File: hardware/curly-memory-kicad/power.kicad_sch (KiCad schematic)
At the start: 19 parts, among them J501 Conn_02x05_Odd_Even, U501 NCP1117-5.0_SOT223, U502 NCP1117-3.3_SOT223

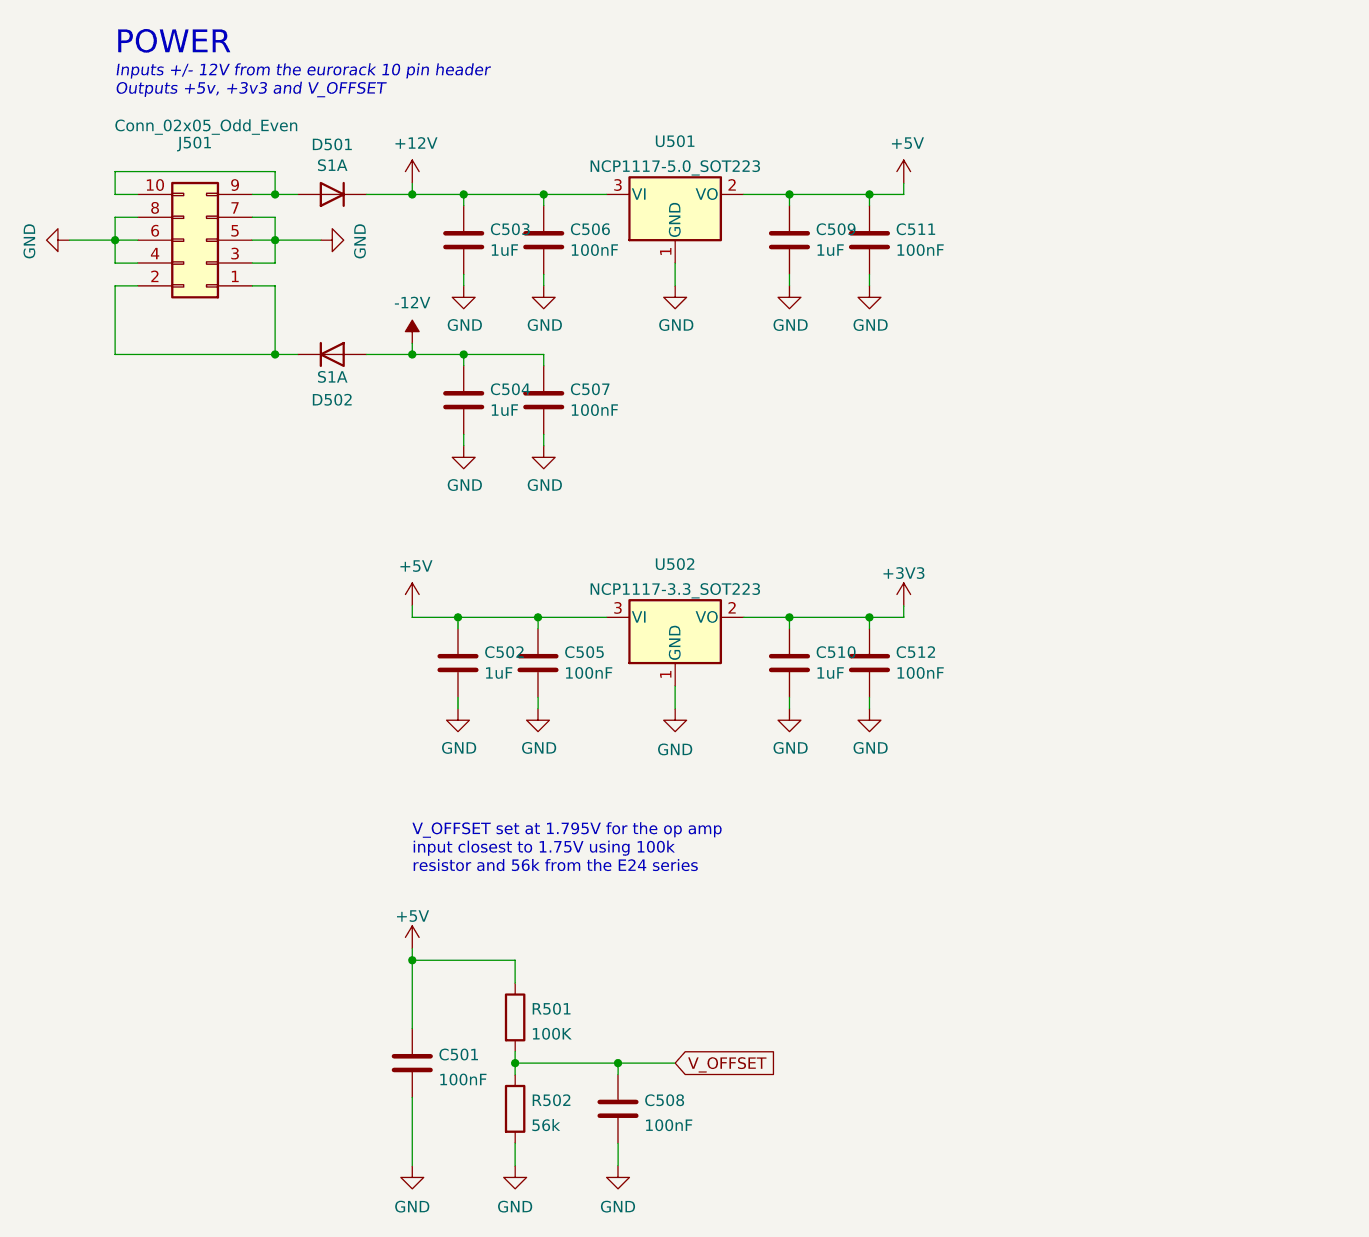
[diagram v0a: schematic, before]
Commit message: all components placed on the main board
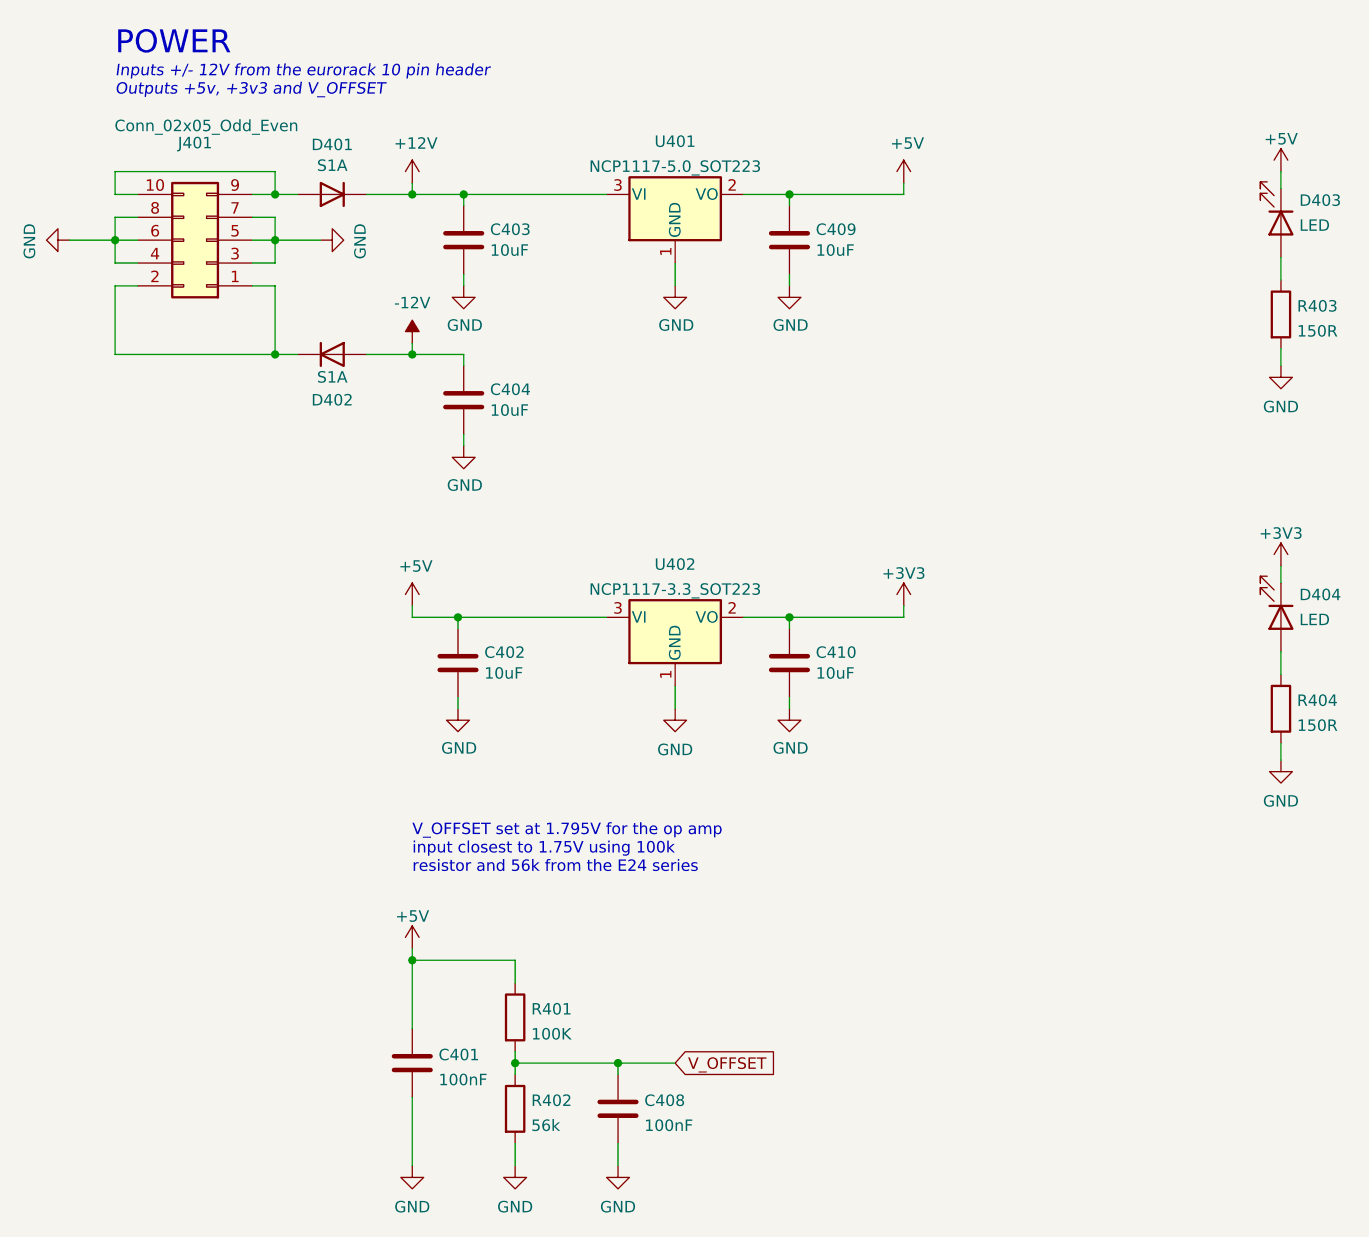
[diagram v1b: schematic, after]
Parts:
- removed C505, C506, C507, C511, C512: 100nF, Capacitor_SMD:C_0805_2012Metric_Pad1.18x1.45mm_HandSolder, symbol Device:C
- added D403, D404: LED, LED_SMD:LED_0805_2012Metric_Pad1.15x1.40mm_HandSolder, symbol Device:LED
- added R403, R404: 150R, Resistor_SMD:R_0805_2012Metric_Pad1.20x1.40mm_HandSolder, symbol Device:R
- C402: renamed from C502; value 1uF -> 10uF
- C403: renamed from C503; value 1uF -> 10uF
- C404: renamed from C504; value 1uF -> 10uF
- C409: renamed from C509; value 1uF -> 10uF
- C410: renamed from C510; value 1uF -> 10uF
- D401: renamed from D501; footprint Diode_SMD:D_SMA-SMB_Universal_Handsoldering -> Diode_SMD:D_SMA_Handsoldering
- D402: renamed from D502; footprint Diode_SMD:D_SMA-SMB_Universal_Handsoldering -> Diode_SMD:D_SMA_Handsoldering
- J401: renamed from J501; footprint Connector_IDC:IDC-Header_2x05_P2.54mm_Vertical -> Connector_IDC:IDC-Header_2x05_P2.54mm_Horizontal
- renumbered C501 to C401, C508 to C408, R501 to R401, R502 to R402, U501 to U401, U502 to U402
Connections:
- net +3V3: now also D404.1 (K)
- net +5V: now also D403.1 (K)
- net GND: now also R403.2, R404.2
- new net: D403.2 (A), R403.1
- new net: D404.2 (A), R404.1

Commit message: silkscreen lined up lovely
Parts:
- D401, D402: footprint Diode_SMD:D_SMA_Handsoldering -> Diode_SMD:D_SMA
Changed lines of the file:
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@@
     (property "Reference" "D401" (id 0) (at 55.88 35.7632 0))
     (property "Value" "S1A" (id 1) (at 55.88 38.0746 0))
-    (property "Footprint" "Diode_SMD:D_SMA_Handsoldering" (id 2) (at 55.88 41.275 0)
+    (property "Footprint" "Diode_SMD:D_SMA" (id 2) (at 55.88 41.275 0)
       (effects (font (size 1.27 1.27)) hide)
     )
@@
     (property "Reference" "D402" (id 0) (at 55.88 64.135 0))
     (property "Value" "S1A" (id 1) (at 55.88 61.595 0))
-    (property "Footprint" "Diode_SMD:D_SMA_Handsoldering" (id 2) (at 55.88 59.055 0)
-      (effects (font (size 1.27 1.27)) hide)
-    )
+    (property "Footprint" "Diode_SMD:D_SMA" (id 2) (at 55.88 59.055 0)
+      (effects (font (size 1.27 1.27)) hide)
+    )

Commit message: gerbers genearted and mf/mfpn added for main board for build
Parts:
- C401, C408: MF (none) -> Samsung; MFPN (none) -> CL21B104KBCNNNC; Material (none) -> X7R; Voltage (none) -> 50V
- C402, C403, C404, C409, C410: MF (none) -> Murata; MFPN (none) -> GRM21BR61H106KE43L; Material (none) -> X5R; Voltage (none) -> 50V
- D403, D404: MF (none) -> Kingbright; MFPN (none) -> KP-2012EC
- J401: now left out of the parts list
- R401: MF (none) -> Multicomp; MFPN (none) -> MCWR08X1003FTL; Tolerance (none) -> 1%
- R402: value 56k -> 56K; MF (none) -> Multicomp; MFPN (none) -> MCWR08X5602FTL; Tolerance (none) -> 1%
- R403, R404: MF (none) -> Multicomp; MFPN (none) -> MCWR08X1500FTL; Tolerance (none) -> 1%
- U401: MF (none) -> STMICROELECTRONICS; MFPN (none) -> LD1117S50TR; Voltage (none) -> 5V
- U402: MF (none) -> STMICROELECTRONICS; MFPN (none) -> LD1117S33TR; Voltage (none) -> 3V3
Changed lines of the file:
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@@
+      (effects (font (size 1.27 1.27)) hide)
+    )
+    (property "Voltage" "50V" (id 4) (at 106.68 93.345 0)
+      (effects (font (size 1.27 1.27)) hide)
+    )
+    (property "MF" "Murata" (id 5) (at 106.68 93.345 0)
+      (effects (font (size 1.27 1.27)) hide)
+    )
+    (property "MFPN" "GRM21BR61H106KE43L " (id 6) (at 106.68 93.345 0)
+      (effects (font (size 1.27 1.27)) hide)
+    )
+    (property "Material" "X5R" (id 7) (at 106.68 93.345 0)
       (effects (font (size 1.27 1.27)) hide)
     )
@@
       (effects (font (size 1.27 1.27)) (justify left))
     )
-    (property "Value" "56k" (id 1) (at 77.978 144.7416 0)
+    (property "Value" "56K" (id 1) (at 77.978 144.7416 0)
       (effects (font (size 1.27 1.27)) (justify left))
     )
@@
       (effects (font (size 1.27 1.27)) hide)
     )
+    (property "MF" "Multicomp" (id 4) (at 76.2 142.875 0)
+      (effects (font (size 1.27 1.27)) hide)
+    )
+    (property "MFPN" "MCWR08X5602FTL " (id 5) (at 76.2 142.875 0)
+      (effects (font (size 1.27 1.27)) hide)
+    )
+    (property "Tolerance" "1%" (id 6) (at 76.2 142.875 0)
+      (effects (font (size 1.27 1.27)) hide)
+    )
     (pin "1")
     (pin "2")
@@
       (effects (font (size 1.27 1.27)) hide)
     )
+    (property "MF" "Kingbright" (id 4) (at 161.29 44.45 90)
+      (effects (font (size 1.27 1.27)) hide)
+    )
+    (property "MFPN" "KP-2012EC" (id 5) (at 161.29 44.45 90)
+      (effects (font (size 1.27 1.27)) hide)
+    )
     (pin "1")
     (pin "2")
@@
       (effects (font (size 1.27 1.27)) hide)
     )
+    (property "Voltage" "50V" (id 4) (at 70.485 46.355 0)
+      (effects (font (size 1.27 1.27)) (justify left) hide)
+    )
+    (property "MF" "Murata" (id 5) (at 70.485 46.355 0)
+      (effects (font (size 1.27 1.27)) hide)
+    )
+    (property "MFPN" "GRM21BR61H106KE43L " (id 6) (at 70.485 46.355 0)
+      (effects (font (size 1.27 1.27)) hide)
+    )
+    (property "Material" "X5R" (id 7) (at 70.485 46.355 0)
+      (effects (font (size 1.27 1.27)) hide)
+    )
     (pin "1")
     (pin "2")
   )
   (symbol (lib_id "Connector_Generic:Conn_02x05_Odd_Even") (at 41.91 46.355 180) (unit 1)
-    (in_bom yes) (on_board yes)
+    (in_bom no) (on_board yes)
     (property "Reference" "J401" (id 0) (at 40.64 35.56 0))
     (property "Value" "Conn_02x05_Odd_Even" (id 1) (at 41.91 33.655 0))
@@
       (effects (font (size 1.27 1.27)) hide)
     )
+    (property "MF" "STMICROELECTRONICS" (id 4) (at 93.98 41.275 0)
+      (effects (font (size 1.27 1.27)) hide)
+    )
+    (property "MFPN" "LD1117S50TR" (id 5) (at 93.98 41.275 0)
+      (effects (font (size 1.27 1.27)) hide)
+    )
+    (property "Voltage" "5V" (id 6) (at 93.98 41.275 0)
+      (effects (font (size 1.27 1.27)) hide)
+    )
     (pin "1")
     (pin "2")
@@
       (effects (font (size 1.27 1.27)) hide)
     )
+    (property "Voltage" "50V" (id 4) (at 64.77 137.795 0)
+      (effects (font (size 1.27 1.27)) hide)
+    )
+    (property "MF" "Samsung" (id 5) (at 64.77 137.795 0)
+      (effects (font (size 1.27 1.27)) hide)
+    )
+    (property "MFPN" "CL21B104KBCNNNC" (id 6) (at 64.77 137.795 0)
+      (effects (font (size 1.27 1.27)) hide)
+    )
+    (property "Material" "X7R" (id 7) (at 64.77 137.795 0)
+      (effects (font (size 1.27 1.27)) hide)
+    )
     (pin "1")
     (pin "2")
@@
       (effects (font (size 1.27 1.27)) hide)
     )
+    (property "MF" "Multicomp" (id 4) (at 161.29 98.425 0)
+      (effects (font (size 1.27 1.27)) hide)
+    )
+    (property "MFPN" "MCWR08X1500FTL " (id 5) (at 161.29 98.425 0)
+      (effects (font (size 1.27 1.27)) hide)
+    )
+    (property "Tolerance" "1%" (id 6) (at 161.29 98.425 0)
+      (effects (font (size 1.27 1.27)) hide)
+    )
     (pin "1")
     (pin "2")
@@
     )
     (property "Datasheet" "~" (id 3) (at 69.85 93.345 0)
+      (effects (font (size 1.27 1.27)) hide)
+    )
+    (property "Voltage" "50V" (id 4) (at 69.85 93.345 0)
+      (effects (font (size 1.27 1.27)) hide)
+    )
+    (property "MF" "Murata" (id 5) (at 69.85 93.345 0)
+      (effects (font (size 1.27 1.27)) hide)
+    )
+    (property "MFPN" "GRM21BR61H106KE43L " (id 6) (at 69.85 93.345 0)
+      (effects (font (size 1.27 1.27)) hide)
+    )
+    (property "Material" "X5R" (id 7) (at 69.85 93.345 0)
       (effects (font (size 1.27 1.27)) hide)
     )
@@
       (effects (font (size 1.27 1.27)) hide)
     )
+    (property "MF" "STMICROELECTRONICS" (id 4) (at 93.98 88.265 0)
+      (effects (font (size 1.27 1.27)) hide)
+    )
+    (property "MFPN" "LD1117S33TR" (id 5) (at 93.98 88.265 0)
+      (effects (font (size 1.27 1.27)) hide)
+    )
+    (property "Voltage" "3V3" (id 6) (at 93.98 88.265 0)
+      (effects (font (size 1.27 1.27)) hide)
+    )
     (pin "1")
     (pin "2")
@@
       (effects (font (size 1.27 1.27)) hide)
     )
+    (property "Voltage" "50V" (id 4) (at 70.485 64.135 0)
+      (effects (font (size 1.27 1.27)) hide)
+    )
+    (property "MF" "Murata" (id 5) (at 70.485 64.135 0)
+      (effects (font (size 1.27 1.27)) hide)
+    )
+    (property "MFPN" "GRM21BR61H106KE43L " (id 6) (at 70.485 64.135 0)
+      (effects (font (size 1.27 1.27)) hide)
+    )
+    (property "Material" "X5R" (id 7) (at 70.485 64.135 0)
+      (effects (font (size 1.27 1.27)) hide)
+    )
     (pin "1")
     (pin "2")
@@
     )
     (property "Datasheet" "~" (id 3) (at 161.29 54.61 0)
+      (effects (font (size 1.27 1.27)) hide)
+    )
+    (property "MF" "Multicomp" (id 4) (at 161.29 54.61 0)
+      (effects (font (size 1.27 1.27)) hide)
+    )
+    (property "MFPN" "MCWR08X1500FTL " (id 5) (at 161.29 54.61 0)
+      (effects (font (size 1.27 1.27)) hide)
+    )
+    (property "Tolerance" "1%" (id 6) (at 161.29 54.61 0)
       (effects (font (size 1.27 1.27)) hide)
     )
@@
       (effects (font (size 1.27 1.27)) hide)
     )
+    (property "Voltage" "50V" (id 4) (at 87.63 142.875 0)
+      (effects (font (size 1.27 1.27)) hide)
+    )
+    (property "MF" "Samsung" (id 5) (at 87.63 142.875 0)
+      (effects (font (size 1.27 1.27)) hide)
+    )
+    (property "MFPN" "CL21B104KBCNNNC" (id 6) (at 87.63 142.875 0)
+      (effects (font (size 1.27 1.27)) hide)
+    )
+    (property "Material" "X7R" (id 7) (at 87.63 142.875 0)
+      (effects (font (size 1.27 1.27)) hide)
+    )
     (pin "1")
     (pin "2")
@@
     )
     (property "Datasheet" "~" (id 3) (at 106.68 46.355 0)
+      (effects (font (size 1.27 1.27)) hide)
+    )
+    (property "Voltage" "50V" (id 4) (at 106.68 46.355 0)
+      (effects (font (size 1.27 1.27)) hide)
+    )
+    (property "MF" "Murata" (id 5) (at 106.68 46.355 0)
+      (effects (font (size 1.27 1.27)) hide)
+    )
+    (property "MFPN" "GRM21BR61H106KE43L " (id 6) (at 106.68 46.355 0)
+      (effects (font (size 1.27 1.27)) hide)
+    )
+    (property "Material" "X5R" (id 7) (at 106.68 46.355 0)
       (effects (font (size 1.27 1.27)) hide)
     )
@@
       (effects (font (size 1.27 1.27)) hide)
     )
+    (property "MF" "Kingbright" (id 4) (at 161.29 88.265 0)
+      (effects (font (size 1.27 1.27)) hide)
+    )
+    (property "MFPN" "KP-2012EC" (id 5) (at 161.29 88.265 0)
+      (effects (font (size 1.27 1.27)) hide)
+    )
     (pin "1")
     (pin "2")
@@
       (effects (font (size 1.27 1.27)) hide)
     )
+    (property "MF" "Multicomp" (id 4) (at 76.2 132.715 0)
+      (effects (font (size 1.27 1.27)) hide)
+    )
+    (property "MFPN" "MCWR08X1003FTL " (id 5) (at 76.2 132.715 0)
+      (effects (font (size 1.27 1.27)) hide)
+    )
+    (property "Tolerance" "1%" (id 6) (at 76.2 132.715 0)
+      (effects (font (size 1.27 1.27)) hide)
+    )
